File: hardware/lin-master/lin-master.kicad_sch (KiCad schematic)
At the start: 13 parts, among them J1 QWIIC Connector, J2 Screw_Terminal_01x03, U1 Arduino_Nano_v3.x, U2 TJA1021T

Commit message: Added I2C Addr lines and level translation
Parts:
- added JP1, JP2, JP3: Solder Jumper, Jumper:SolderJumper-2_P1.3mm_Open_TrianglePad1.0x1.5mm, symbol Jumper:SolderJumper_2_Open
- added Q1, Q2: 2N7002, Package_TO_SOT_SMD:SOT-23, symbol Transistor_FET:2N7002
- added R10, R11, R12, R8, R9: 10k, Resistor_SMD:R_0805_2012Metric_Pad1.20x1.40mm_HandSolder, symbol Device:R
- renumbered J2 to J1, J1 to J2
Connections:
- net +3V3: now also J2.2 (VCC), R11.1, R12.1
- net +5V: now also R10.1, R8.1, R9.1; no longer J2.2 (VCC)
- net GND: now also JP1.1 (A), JP2.1 (A), JP3.1 (A)
- net A0: now reaches U1.10 (D7)
- net A0: now also JP1.2 (B), R8.2
- net A1: now reaches U1.11 (D8)
- net A1: now also JP2.2 (B), R9.2
- net A2: now reaches U1.12 (D9)
- net A2: now also JP3.2 (B), R10.2
- net SCL5 renamed SCL5V
- net SCL5V: now also Q1.3 (D); no longer J2.4 (SCL)
- net SDA5 renamed SDA5V
- net SDA5V: now also Q2.3 (D); no longer J2.3 (SDA)
- new net SCL3V: J2.4 (SCL), Q1.1 (G), Q1.2 (S), R12.2
- new net SDA3V: J2.3 (SDA), Q2.1 (G), Q2.2 (S), R11.2
- no-connect marks 19 -> 16
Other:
- note added: "I2C Slave Addresses: 0x70-0x77 - EEPROM, 0x78-0x7F - LinBus Bridge bottom 3 bits from A2-A0"
- moved on the sheet: J2

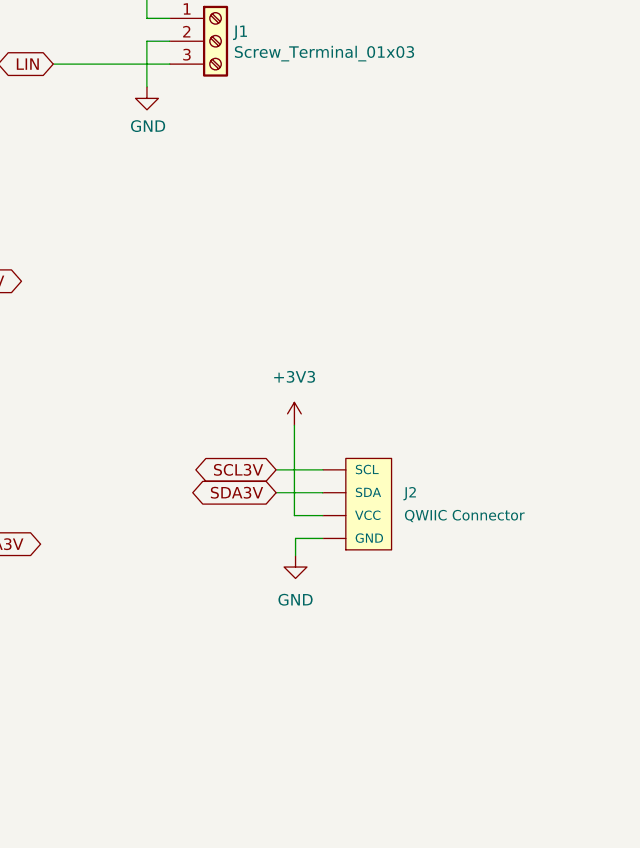
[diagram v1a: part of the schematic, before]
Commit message: Added firmware for lin-master
- also added I2C address selection, and built-in 3.3V->5V translation
  and a second QWIIC connector.
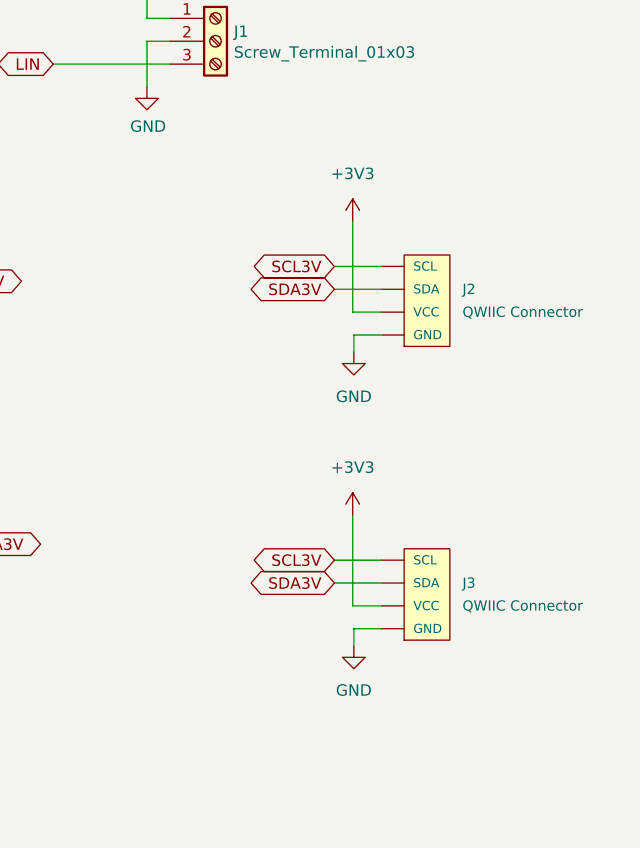
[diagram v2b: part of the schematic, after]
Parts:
- added J2: QWIIC Connector, SparkFun-Connectors:1X04_1MM_RA, symbol SparkFun-Connectors:I2C_STANDARDQWIIC
- renumbered J2 to J3
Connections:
- net +3V3: now also J2.2 (VCC)
- net GND: now also J2.1 (GND)
- net SCL3V: now also J2.4 (SCL)
- net SDA3V: now also J2.3 (SDA)
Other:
- moved on the sheet: J3
